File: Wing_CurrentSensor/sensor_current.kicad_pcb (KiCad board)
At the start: 2 copper layers, 50.8 x 22.9 mm, 25 parts, among them J1 feather long, J2 feather short, J3 SJ-3524-SMT, U1 TL084, U2 AD8226

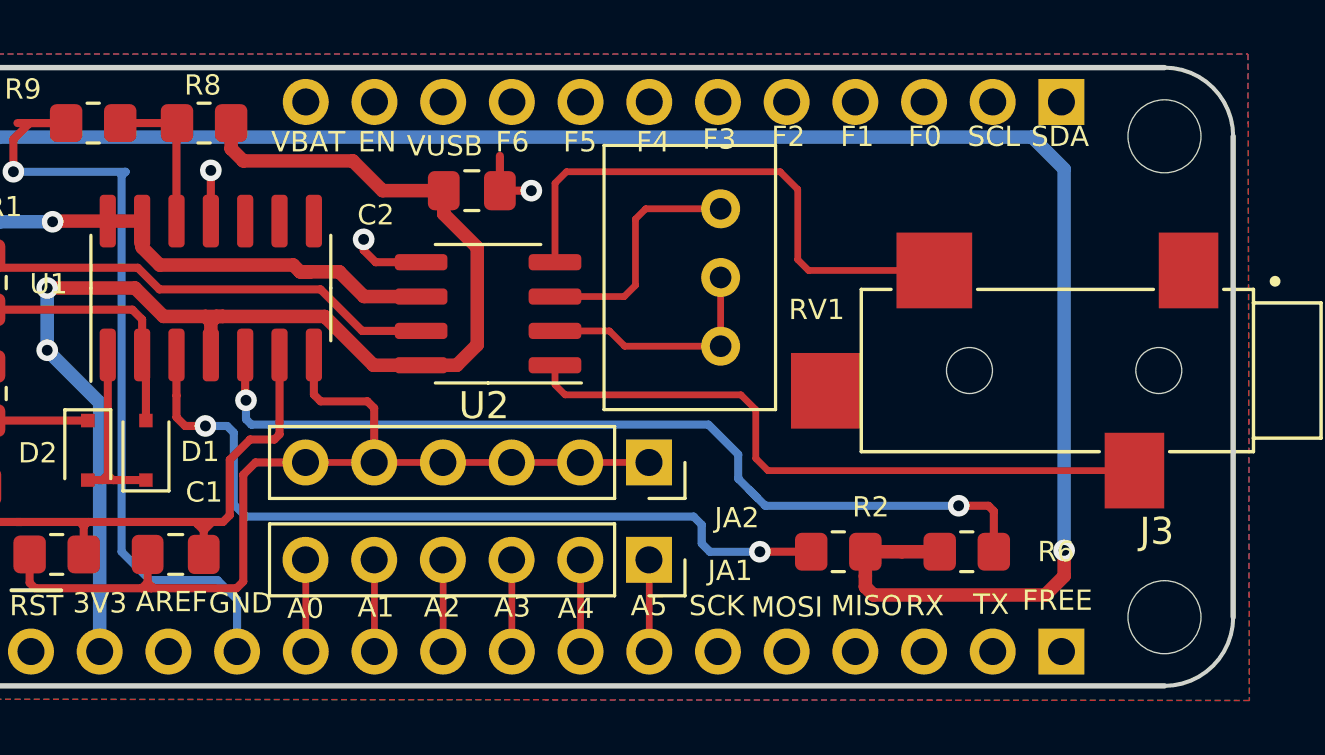
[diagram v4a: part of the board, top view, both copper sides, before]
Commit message: add logos
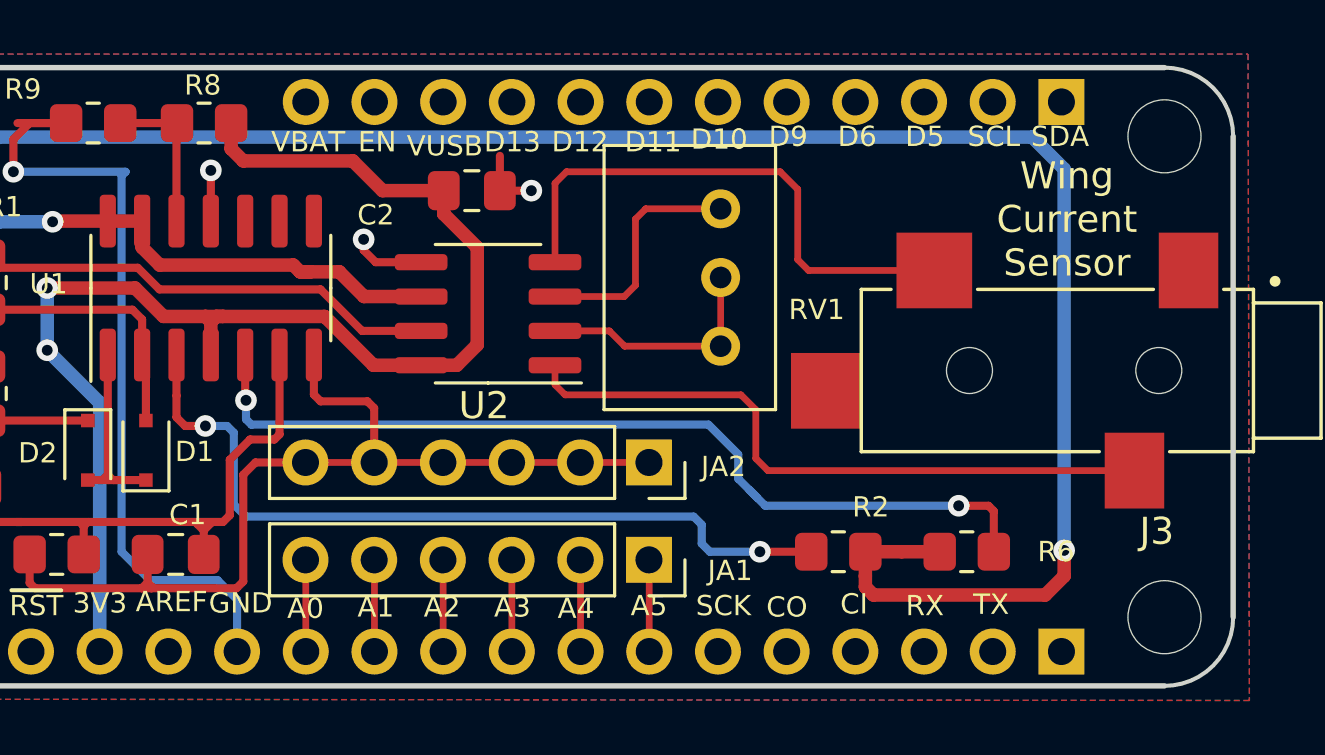
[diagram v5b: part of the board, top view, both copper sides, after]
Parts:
- added G***: LOGO, Aesthetics:electronic_cats_logo_8x6, B.Cu at (144.5, 101.6)
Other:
- board text added: "CI"
- board text added: "CO"
- board text added: "D10"
- board text added: "D11"
- board text added: "D12"
- board text added: "D13"
- board text added: "D5"
- board text added: "D6"
- board text added: "D9"
- board text added: "Wing Current Sensor"
- board text added: "Wing Current Sensor V1.0"
- board text removed: "F0"
- board text removed: "F1"
- board text removed: "F2"
- board text removed: "F3"
- board text removed: "F4"
- board text removed: "F5"
- board text removed: "F6"
- board text removed: "FREE"
- board text removed: "MISO"
- board text removed: "MOSI"

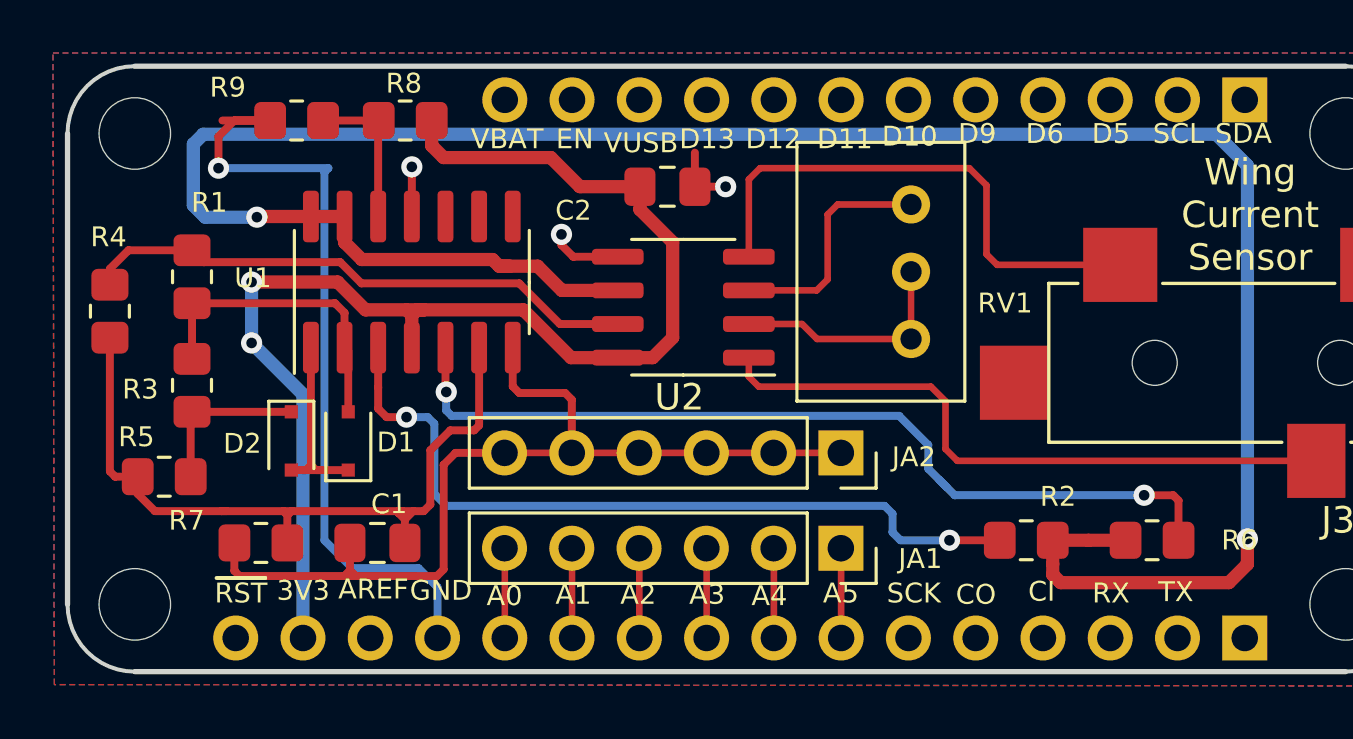
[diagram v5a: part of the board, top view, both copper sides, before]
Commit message: update connecotr for jumpers
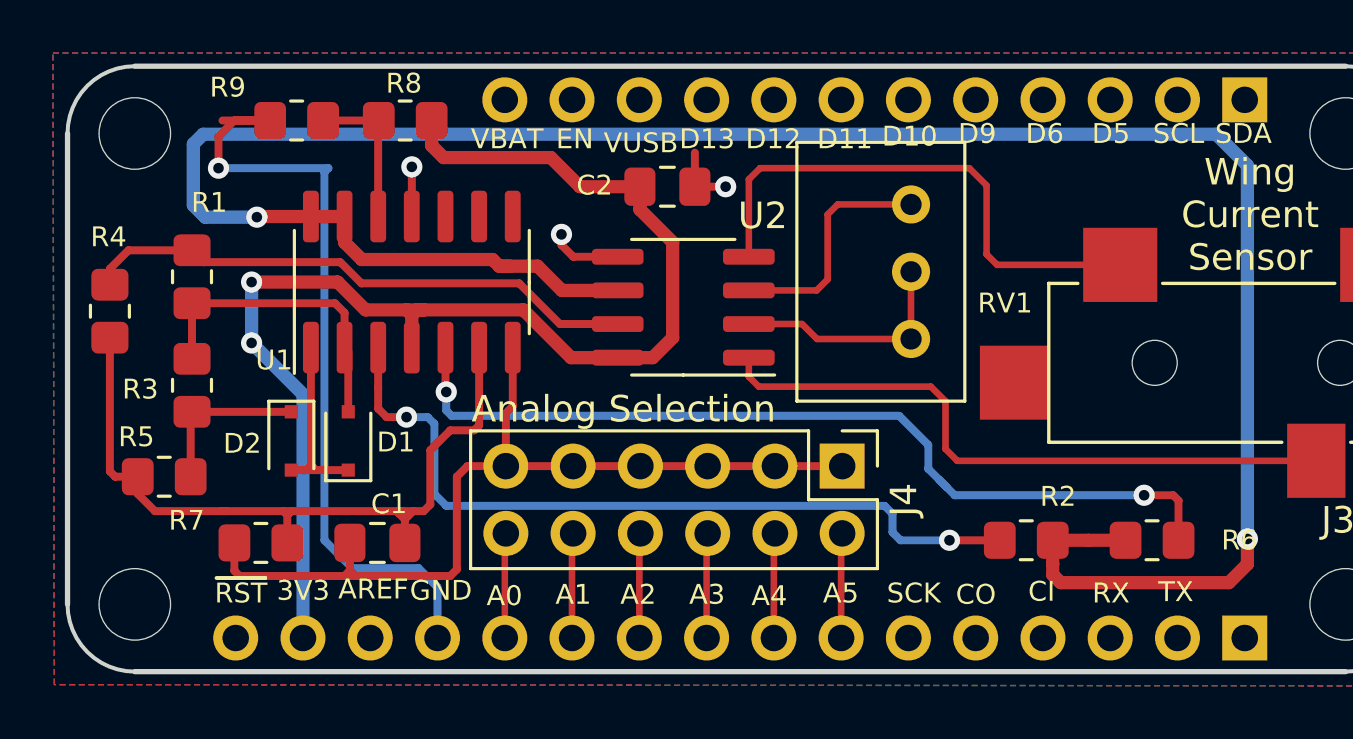
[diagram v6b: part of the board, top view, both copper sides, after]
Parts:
- removed JA1, JA2: Conn_01x06, Connector_PinSocket_2.54mm:PinSocket_1x06_P2.54mm_Vertical
- added J4: Analog Selection, Connector_PinHeader_2.54mm:PinHeader_2x06_P2.54mm_Vertical, F.Cu at (137.2, 105.5)
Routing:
- net /OUT: track 35.8 -> 34.9 mm
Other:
- rule pad_to_mask_clearance: 0.051 -> 0

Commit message: update traces
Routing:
- net GND: track 37.4 -> 11.2 mm
- net /A4: track 3.39 -> 7.36 mm
- net /A1: track 3.39 -> 7.36 mm
- net /A0: track 3.39 -> 7.36 mm
- net /A5: track 3.39 -> 7.36 mm
- net /A3: track 3.39 -> 7.36 mm
- net /A2: track 3.39 -> 7.36 mm
- net /VREF: track 88.0 -> 86.2 mm
- net +3V3: track 59.0 -> 58.1 mm, vias 2 -> 1

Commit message: Add_Connector
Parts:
- moved J3 4.50 mm to (159.2, 104.8)
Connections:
- J3 pad 1: Net-(J3-Pad1) -> GND
- J3 pad 2: /IN+ -> Net-(J3-Pad2)
- J3 pad 3: /IN- -> /IN+
- U2 pad 1: /IN- -> GND
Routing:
- net GND: track 11.2 -> 36.6 mm
- net /IN-: track 24.5 -> 0.00 mm
- net /IN+: track 20.2 -> 21.5 mm
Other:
- net class Default: trace_width 0.3 -> 0.25
